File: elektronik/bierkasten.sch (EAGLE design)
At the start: 71 parts, among them Q1 BC547B

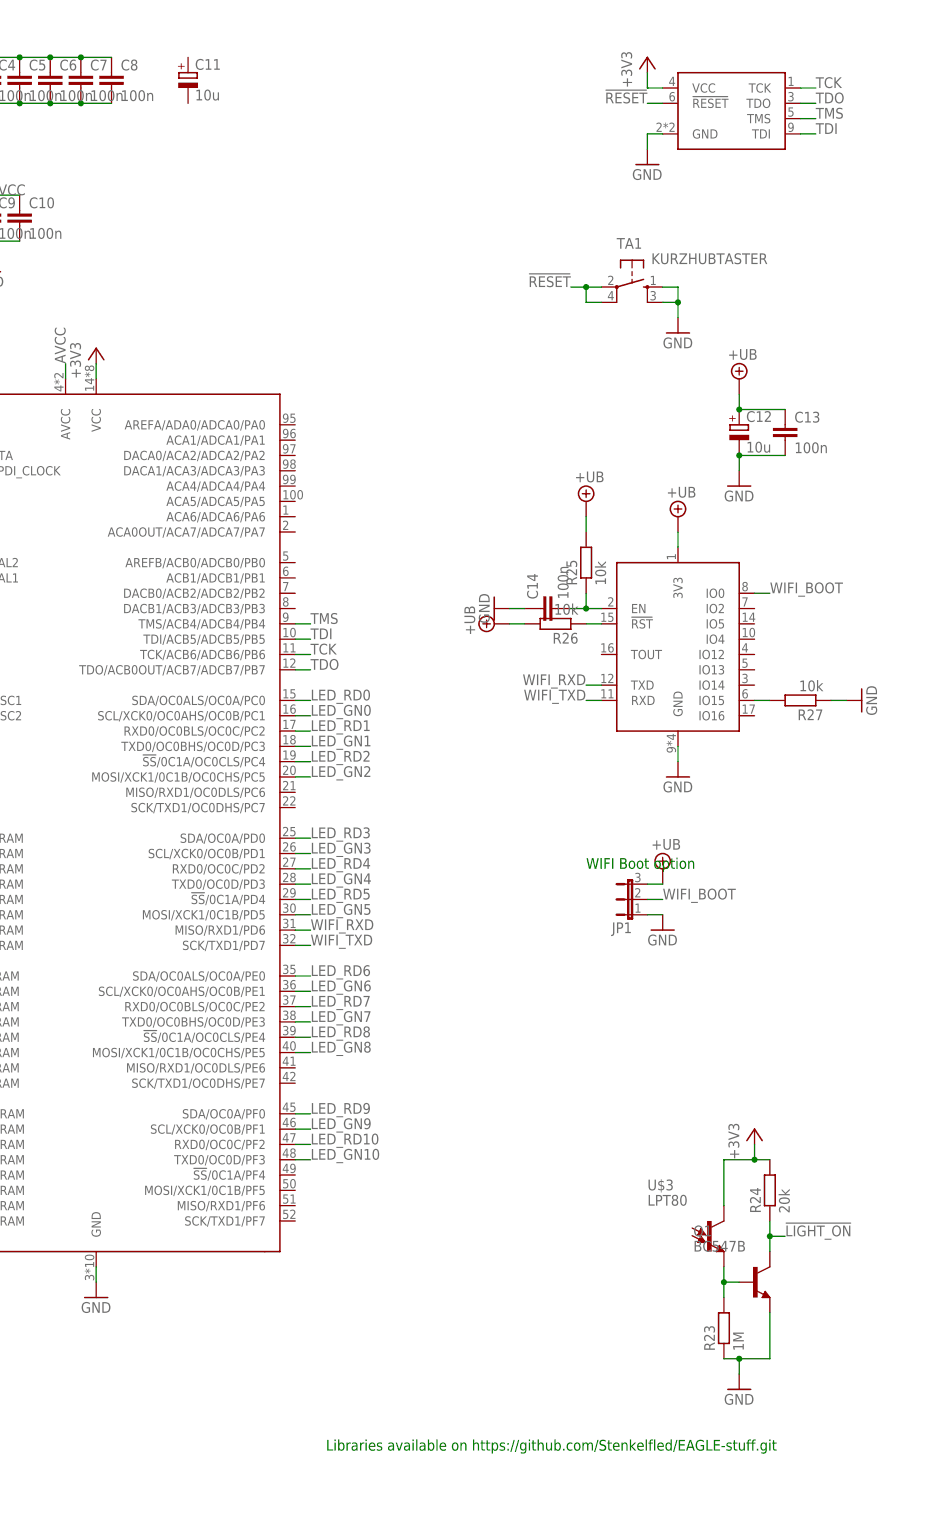
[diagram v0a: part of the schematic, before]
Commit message: Bestellcodes fertig gemacht
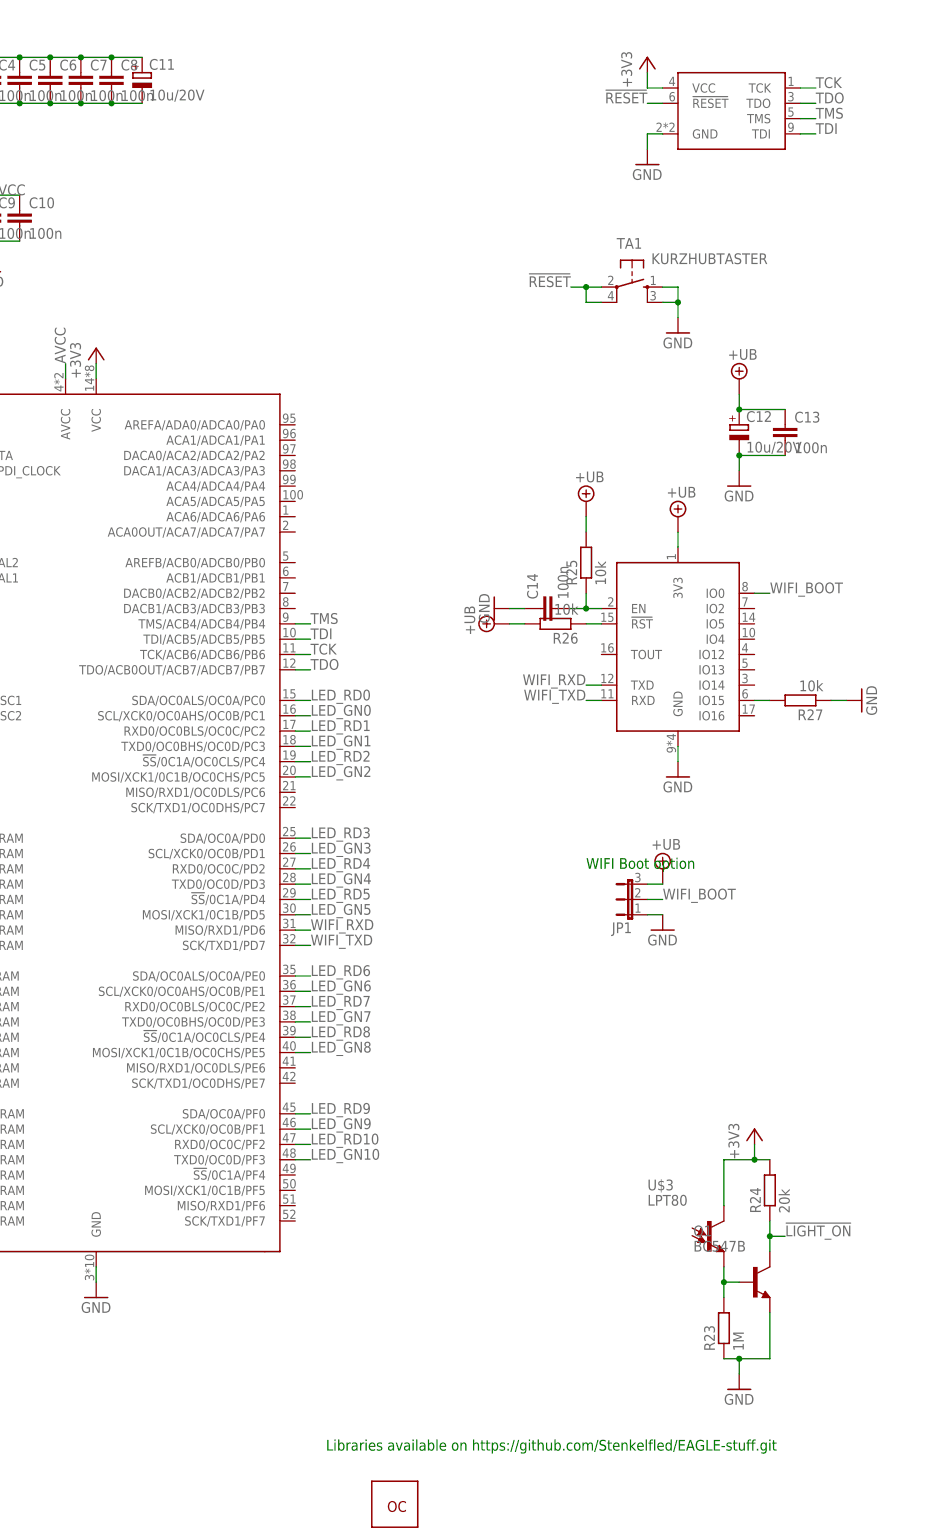
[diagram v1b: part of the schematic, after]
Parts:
- added U$17: BESTELLTEILE, misc_STE:BESTELLTEILE
- C11, C12: value 10u -> 10u/20V; REICHELT (none) -> TAJ 3528 10/20
- FERRITE1: REICHELT (none) -> BLM21PG 331
- Q1: REICHELT (none) -> BC 547B
- R25, R26, R27: FARNELL (none) -> 2502397; REICHELT (none) -> RND 0603 1 10K
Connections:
- net +3V3: now also C11.+
- net GND: now also C11.-
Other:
- moved on the sheet: C11
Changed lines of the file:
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@@
 </part>
 <part name="GND3" library="supply1" library_urn="urn:adsk.eagle:library:371" deviceset="GND" device=""/>
-<part name="FERRITE1" library="ferrite_STE" deviceset="FERRITE-EU_0805" device=""/>
+<part name="FERRITE1" library="ferrite_STE" deviceset="FERRITE-EU_0805" device="">
+<attribute name="REICHELT" value="BLM21PG 331"/>
+</part>
 <part name="+3V2" library="supply1" library_urn="urn:adsk.eagle:library:371" deviceset="+3V3" device=""/>
 <part name="U$2" library="con_STE" deviceset="AVR-JTAG" device="-10">
@@
 <part name="FRAME2" library="frames" library_urn="urn:adsk.eagle:library:229" deviceset="A4P-LOC" device=""/>
 <part name="FRAME3" library="frames" library_urn="urn:adsk.eagle:library:229" deviceset="A4P-LOC" device=""/>
-<part name="Q1" library="transistor-npn" library_urn="urn:adsk.eagle:library:398" deviceset="BC547*" device="" package3d_urn="urn:adsk.eagle:package:28523/2" technology="B"/>
+<part name="Q1" library="transistor-npn" library_urn="urn:adsk.eagle:library:398" deviceset="BC547*" device="" package3d_urn="urn:adsk.eagle:package:28523/2" technology="B">
+<attribute name="REICHELT" value="BC 547B"/>
+</part>
 <part name="U$3" library="misc_STE" deviceset="LPT80" device="">
 <attribute name="REICHELT" value="LPT 80"/>
@@
 </part>
 <part name="GND28" library="supply1" library_urn="urn:adsk.eagle:library:371" deviceset="GND" device=""/>
-<part name="U$15" library="misc_STE" deviceset="ESP8266" device="-POLLIN"/>
-<part name="C11" library="rcl" library_urn="urn:adsk.eagle:library:334" deviceset="CPOL-EU" device="B/3528-21W" package3d_urn="urn:adsk.eagle:package:23411/1" value="10u"/>
-<part name="C12" library="rcl" library_urn="urn:adsk.eagle:library:334" deviceset="CPOL-EU" device="B/3528-21W" package3d_urn="urn:adsk.eagle:package:23411/1" value="10u"/>
+<part name="U$15" library="misc_STE" deviceset="ESP8266" device="-POLLIN">
+<attribute name="NOORDER" value=""/>
+</part>
+<part name="C11" library="rcl" library_urn="urn:adsk.eagle:library:334" deviceset="CPOL-EU" device="B/3528-21W" package3d_urn="urn:adsk.eagle:package:23411/1" value="10u/20V">
+<spice>
+<pinmapping spiceprefix="C">
+<pinmap gate="G$1" pin="+" pinorder="1"/>
+<pinmap gate="G$1" pin="-" pinorder="2"/>
+</pinmapping>
+</spice>
+<attribute name="REICHELT" value="TAJ 3528 10/20"/>
+</part>
+<part name="C12" library="rcl" library_urn="urn:adsk.eagle:library:334" deviceset="CPOL-EU" device="B/3528-21W" package3d_urn="urn:adsk.eagle:package:23411/1" value="10u/20V">
+<spice>
+<pinmapping spiceprefix="C">
+<pinmap gate="G$1" pin="+" pinorder="1"/>
+<pinmap gate="G$1" pin="-" pinorder="2"/>
+</pinmapping>
+</spice>
+<attribute name="REICHELT" value="TAJ 3528 10/20"/>
+</part>
 <part name="C13" library="rcl_STE" deviceset="C-EU" device="C0603" package3d_urn="urn:adsk.eagle:package:23616/2" value="100n">
 <spice>
@@
 <part name="GND31" library="supply1" library_urn="urn:adsk.eagle:library:371" deviceset="GND" device=""/>
 <part name="GND32" library="supply1" library_urn="urn:adsk.eagle:library:371" deviceset="GND" device=""/>
-<part name="JP1" library="jumper" library_urn="urn:adsk.eagle:library:252" deviceset="JP2E" device="" package3d_urn="urn:adsk.eagle:package:15452/1"/>
+<part name="JP1" library="jumper" library_urn="urn:adsk.eagle:library:252" deviceset="JP2E" device="" package3d_urn="urn:adsk.eagle:package:15452/1">
+<attribute name="NOORDER" value=""/>
+</part>
 <part name="SUPPLY1" library="supply2" library_urn="urn:adsk.eagle:library:372" deviceset="+UB" device=""/>
 <part name="SUPPLY2" library="supply2" library_urn="urn:adsk.eagle:library:372" deviceset="+UB" device=""/>
@@
 </pinmapping>
 </spice>
+<attribute name="FARNELL" value="2502397"/>
+<attribute name="REICHELT" value="RND 0603 1 10K"/>
 </part>
 <part name="R26" library="rcl" library_urn="urn:adsk.eagle:library:334" deviceset="R-EU_" device="R0603" package3d_urn="urn:adsk.eagle:package:23555/2" value="10k">
@@
 </pinmapping>
 </spice>
+<attribute name="FARNELL" value="2502397"/>
+<attribute name="REICHELT" value="RND 0603 1 10K"/>
 </part>
 <part name="R27" library="rcl" library_urn="urn:adsk.eagle:library:334" deviceset="R-EU_" device="R0603" package3d_urn="urn:adsk.eagle:package:23555/2" value="10k">
@@
 </pinmapping>
 </spice>
+<attribute name="FARNELL" value="2502397"/>
+<attribute name="REICHELT" value="RND 0603 1 10K"/>
 </part>
 <part name="GND33" library="supply1" library_urn="urn:adsk.eagle:library:371" deviceset="GND" device=""/>
+<part name="U$17" library="misc_STE" deviceset="BESTELLTEILE" device="">
+<attribute name="REICHELT" value="SL 1X36G 2,54:JUMPER 2,54 GN*10"/>
+</part>
 </parts>
 <sheets>
@@
 </instance>
 <instance part="C8" gate="G$1" x="50.8" y="248.92">
+<attribute name="REICHELT" x="50.8" y="248.92" size="1.778" layer="96" display="off"/>
 <attribute name="FARNELL" x="50.8" y="248.92" size="1.778" layer="96" display="off"/>
-<attribute name="REICHELT" x="50.8" y="248.92" size="1.778" layer="96" display="off"/>
 </instance>
 <instance part="C9" gate="G$1" x="30.48" y="226.06">
@@
 </instance>
 <instance part="GND3" gate="1" x="30.48" y="215.9"/>
-<instance part="FERRITE1" gate="G$1" x="22.86" y="228.6"/>
+<instance part="FERRITE1" gate="G$1" x="22.86" y="228.6">
+<attribute name="REICHELT" x="22.86" y="228.6" size="1.778" layer="96" display="off"/>
+</instance>
 <instance part="+3V2" gate="G$1" x="15.24" y="233.68"/>
 <instance part="U$2" gate="G$1" x="154.94" y="243.84">
@@
 <instance part="FRAME2" gate="G$1" x="185.42" y="0"/>
 <instance part="FRAME3" gate="G$1" x="0" y="0"/>
-<instance part="Q1" gate="G$1" x="157.48" y="48.26"/>
+<instance part="Q1" gate="G$1" x="157.48" y="48.26">
+<attribute name="REICHELT" x="157.48" y="48.26" size="1.778" layer="96" display="off"/>
+</instance>
 <instance part="U$3" gate="G$1" x="149.86" y="55.88">
 <attribute name="REICHELT" x="149.86" y="55.88" size="1.778" layer="96" display="off"/>
@@
 </instance>
 <instance part="GND28" gate="1" x="144.78" y="205.74"/>
-<instance part="U$15" gate="G$1" x="144.78" y="152.4"/>
-<instance part="C11" gate="G$1" x="63.5" y="248.92"/>
-<instance part="C12" gate="G$1" x="154.94" y="190.5"/>
+<instance part="U$15" gate="G$1" x="144.78" y="152.4">
+<attribute name="NOORDER" x="144.78" y="152.4" size="1.778" layer="96" display="off"/>
+</instance>
+<instance part="C11" gate="G$1" x="55.88" y="248.92">
+<attribute name="REICHELT" x="55.88" y="248.92" size="1.778" layer="96" display="off"/>
+</instance>
+<instance part="C12" gate="G$1" x="154.94" y="190.5">
+<attribute name="REICHELT" x="154.94" y="190.5" size="1.778" layer="96" display="off"/>
+</instance>
 <instance part="C13" gate="G$1" x="162.56" y="190.5">
 <attribute name="FARNELL" x="162.56" y="190.5" size="1.778" layer="96" display="off"/>
@@
 <instance part="GND31" gate="1" x="114.3" y="160.02" rot="R270"/>
 <instance part="GND32" gate="1" x="175.26" y="144.78" rot="R90"/>
-<instance part="JP1" gate="1" x="137.16" y="111.76" rot="R90"/>
+<instance part="JP1" gate="1" x="137.16" y="111.76" rot="R90">
+<attribute name="NOORDER" x="137.16" y="111.76" size="1.778" layer="96" rot="R90" display="off"/>
+</instance>
 <instance part="SUPPLY1" gate="G$1" x="154.94" y="198.12"/>
 <instance part="SUPPLY2" gate="G$1" x="144.78" y="175.26"/>
@@
 <instance part="SUPPLY4" gate="G$1" x="142.24" y="116.84"/>
 <instance part="SUPPLY5" gate="G$1" x="114.3" y="157.48" rot="R90"/>
-<instance part="R25" gate="G$1" x="129.54" y="167.64" rot="R90"/>
-<instance part="R26" gate="G$1" x="124.46" y="157.48" rot="R180"/>
-<instance part="R27" gate="G$1" x="165.1" y="144.78" rot="R180"/>
+<instance part="R25" gate="G$1" x="129.54" y="167.64" rot="R90">
+<attribute name="FARNELL" x="129.54" y="167.64" size="1.778" layer="96" display="off"/>
+<attribute name="REICHELT" x="129.54" y="167.64" size="1.778" layer="96" display="off"/>
+</instance>
+<instance part="R26" gate="G$1" x="124.46" y="157.48" rot="R180">
+<attribute name="FARNELL" x="124.46" y="157.48" size="1.778" layer="96" display="off"/>
+<attribute name="REICHELT" x="124.46" y="157.48" size="1.778" layer="96" display="off"/>
+</instance>
+<instance part="R27" gate="G$1" x="165.1" y="144.78" rot="R180">
+<attribute name="FARNELL" x="165.1" y="144.78" size="1.778" layer="96" display="off"/>
+<attribute name="REICHELT" x="165.1" y="144.78" size="1.778" layer="96" display="off"/>
+</instance>
 <instance part="GND33" gate="1" x="142.24" y="106.68"/>
+<instance part="U$17" gate="G$1" x="96.52" y="10.16">
+<attribute name="REICHELT" x="96.52" y="10.16" size="1.778" layer="96" display="off"/>
+</instance>
 </instances>
 <busses>
@@
 <wire x1="15.24" y1="251.46" x2="15.24" y2="254" width="0.1524" layer="91"/>
 <junction x="15.24" y="251.46"/>
+<pinref part="C11" gate="G$1" pin="+"/>
+<wire x1="50.8" y1="251.46" x2="55.88" y2="251.46" width="0.1524" layer="91"/>
+<junction x="50.8" y="251.46"/>
 </segment>
 <segment>
@@
 <wire x1="45.72" y1="243.84" x2="50.8" y2="243.84" width="0.1524" layer="91"/>
 <junction x="45.72" y="243.84"/>
+<pinref part="C11" gate="G$1" pin="-"/>
+<wire x1="55.88" y1="243.84" x2="50.8" y2="243.84" width="0.1524" layer="91"/>
+<junction x="50.8" y="243.84"/>
 </segment>
 <segment>
